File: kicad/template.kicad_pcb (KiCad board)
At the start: 2 copper layers, 84.1 x 61.7 mm, 45 parts, among them J1 Bus_PCI_Express_x1, J4 Conn_01x04_Socket, J5 TF-115-BCP9, J6 USB_C_Receptacle_USB2.0_16P, U1 MCP25625T-E/ML, U2 RP2040, U4 W25Q128JVP, X1 ABM8-272-T3, Y1 X322516MLB4SI

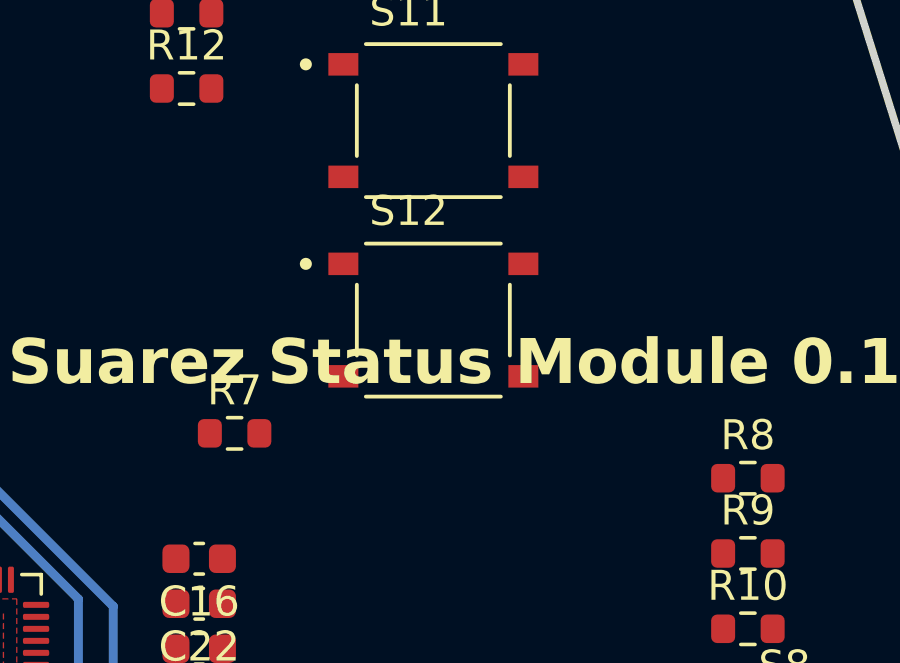
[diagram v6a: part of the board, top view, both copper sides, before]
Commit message: update schematic
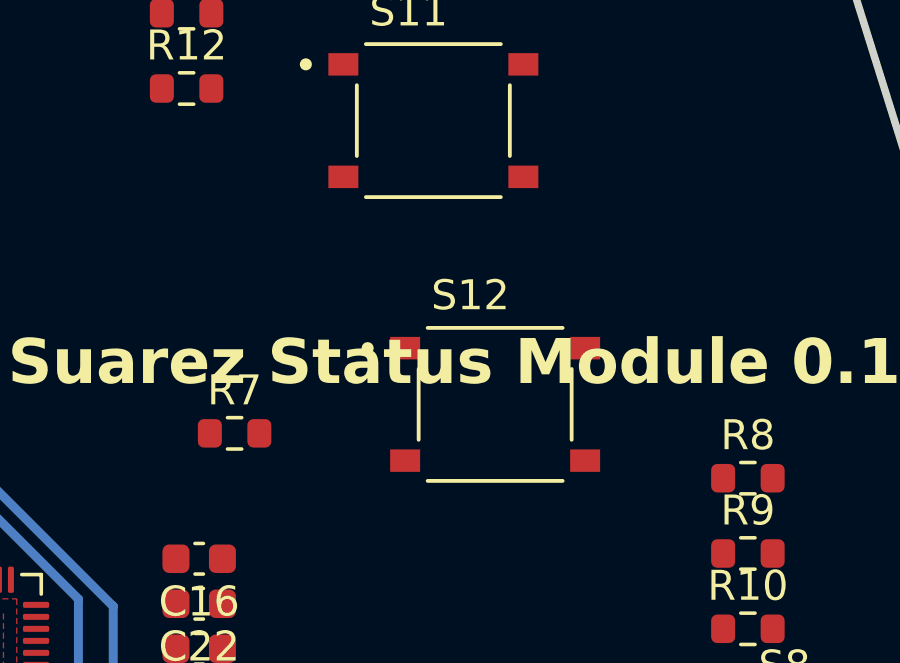
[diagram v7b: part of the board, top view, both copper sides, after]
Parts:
- moved S12 3.48 mm to (165.8, 89.0)
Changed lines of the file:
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@@
 	(footprint "Nicolas Library:SW_TS-1187A-B-A-B"
 		(layer "F.Cu")
-		(at 163.78 86.22)
+		(at 165.84 89.03)
 		(property "Reference" "S12"
 			(at -0.825 -3.635 0)

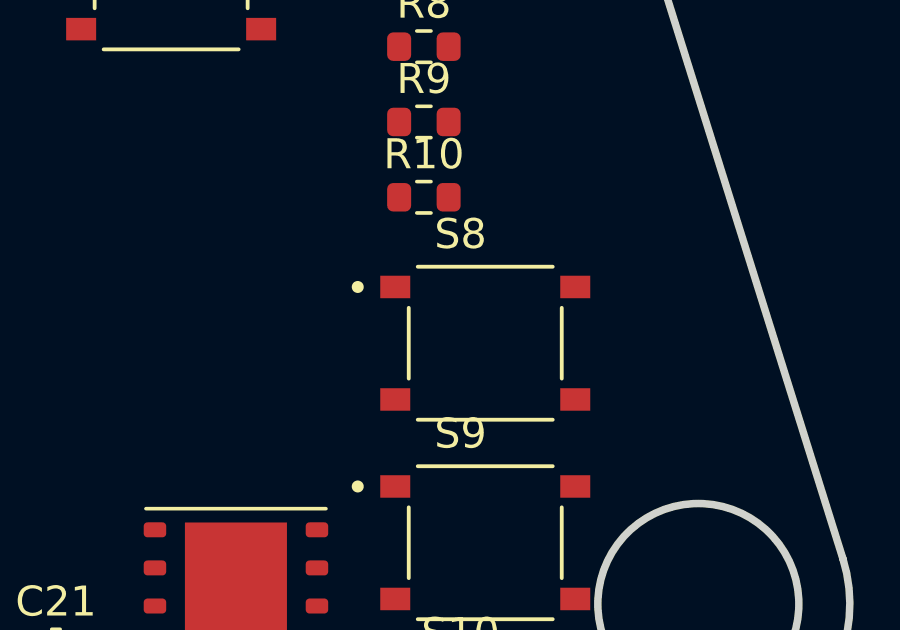
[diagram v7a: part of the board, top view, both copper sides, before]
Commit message: update schematic
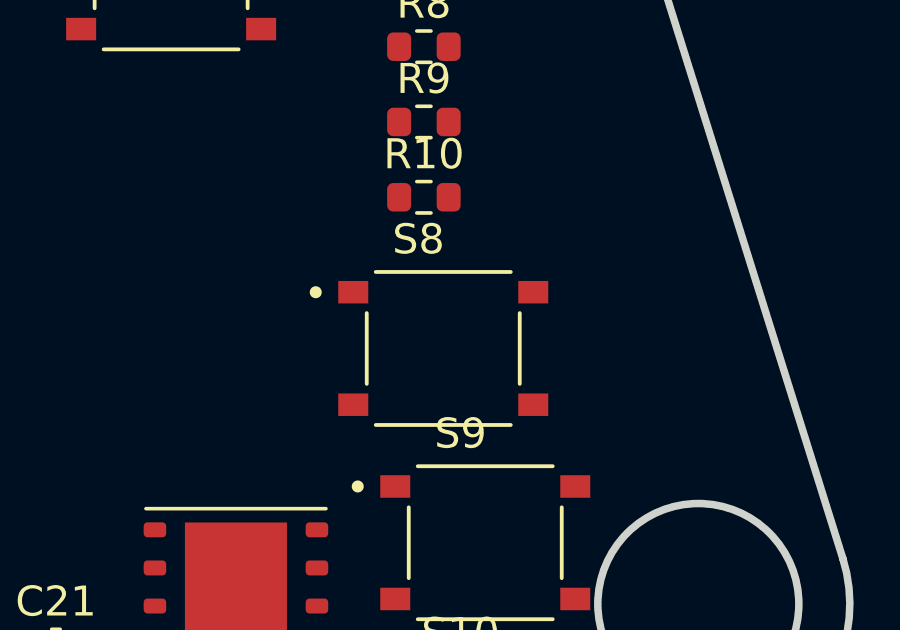
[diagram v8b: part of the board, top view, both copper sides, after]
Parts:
- moved S8 1.41 mm to (174.9, 101.5)
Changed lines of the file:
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@@
 	(footprint "Nicolas Library:SW_TS-1187A-B-A-B"
 		(layer "F.Cu")
-		(at 176.31 101.375)
+		(at 174.91 101.55)
 		(property "Reference" "S8"
 			(at -0.825 -3.635 0)
